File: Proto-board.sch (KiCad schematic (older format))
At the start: 82 parts, among them J1 Conn_01x02, J2 Conn_01x06, J3 Conn_01x05, J4 Conn_01x05, J5 Conn_01x05, J6 Conn_01x05, J7 Conn_01x16, J9 Conn_02x06_Odd_Even, SW1 9001-XX-00, SW10 9001-XX-00, SW11 9001-XX-00, SW12 9001-XX-00, SW13 9001-XX-00, SW14 9001-XX-00, SW15 9001-XX-00, SW16 9001-XX-00, SW17 9001-XX-00, SW18 9001-XX-00, SW19 9001-XX-00, SW2 9001-XX-00, SW20 9001-XX-00, SW3 9001-XX-00, SW4 9001-XX-00, SW5 9001-XX-00, SW6 9001-XX-00, SW7 9001-XX-00, SW8 9001-XX-00, SW9 9001-XX-00, U1 TPL7407LA, U2 MAX17502, U3 XC2C128-VQ100, U4 TPL7407LA, U5 TPL7407LA, U6 MAX15027

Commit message: Final version of protoboard prior to major revision.
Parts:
- added TPA1, TPA2, TPB1, TPB2, TPC1, TPC2, TPD1, TPD2: TEST, Measurement_Points:Measurement_Point_Round-TH_Small, symbol TEST
- C1, C11, C12, C13, C14, C18, C2, C3, C4, C5, C6: footprint Capacitors_SMD:C_1206_HandSoldering -> passives_IKM:1206_PROTO
- J7: footprint Pin_Headers:Pin_Header_Straight_1x16_Pitch2.54mm -> Pin_Headers:Pin_Header_Straight_2x08_Pitch2.00mm_SMD
- L1: footprint Inductors_SMD:L_Coilcraft_XAL5030 -> coilcraft_IKM:LPS6235
- R1, R2, R3, R4: footprint Resistors_SMD:R_1206_HandSoldering -> Resistors_SMD:R_0805
- U2: footprint Housings_DFN_QFN:DFN-10-1EP_3x3mm_Pitch0.5mm -> Housings_DFN_QFN:DFN-10-1EP_2x3mm_Pitch0.5mm
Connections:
- net GNDREF: no longer J3.5 (Pin_5), J4.5 (Pin_5), J5.5 (Pin_5), J6.5 (Pin_5)
- new net GNDS: J3.5 (Pin_5), J4.5 (Pin_5), J5.5 (Pin_5), J6.5 (Pin_5)
- new net TA+: TPA1.1, TPA2.1
- new net TA-: TPB1.1, TPB2.1
- new net TB+: TPC1.1, TPC2.1
- new net TB-: TPD1.1, TPD2.1
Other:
- note added: "Perhaps need to add 100 ohm \nfeedback resistor from 3V3 to FB/VO\n\nMay consider LC filter(s)\n\nLook at INPUT noise from PS"

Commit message: Second version (4x6 card) revC, which was ordered.
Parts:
- removed D11, D12, D13, D14, D15, D16, D17, D18, D19, D20: LED, LEDs:LED_0603_HandSoldering, symbol LED
- removed J1: Conn_01x02, Pin_Headers:Pin_Header_Straight_1x02_Pitch2.54mm, symbol Conn_01x02
- removed J3, J4, J5, J6: Conn_01x05, Pin_Headers:Pin_Header_Straight_1x05_Pitch2.54mm, symbol Conn_01x05
- removed J7: Conn_01x16, Pin_Headers:Pin_Header_Straight_2x08_Pitch2.00mm_SMD, symbol Conn_01x16
- removed J9: Conn_02x06_Odd_Even, Pin_Headers:Pin_Header_Straight_2x06_Pitch2.54mm, symbol Conn_02x06_Odd_Even
- removed RN3: R_Pack08, resistor_array_IKM:SOIC-16, symbol R_Pack08
- added C20, C21, C22: 0.1uF, passives_IKM:1206_PROTO, symbol C
- added C23, C24: CP, Capacitors_SMD:CP_Elec_6.3x4.5, symbol CP
- added J1, J3, J8, J9: Conn_01x08, Connectors_IDC:IDC-Header_2x04_Pitch2.54mm_Straight, symbol Conn_01x08
- added J11, J12, J13, J14, J15, J16, J17, J19: Conn_01x02, Pin_Headers:Pin_Header_Straight_1x02_Pitch2.54mm, symbol Conn_01x02
- added J18: DB37_Female, dsub_IKM:DC37_F_Straddle, symbol DB37_Female
- added J4: Conn_02x20_Odd_Even, Connectors_IDC:IDC-Header_2x20_Pitch2.54mm_Angled, symbol Conn_02x20_Odd_Even
- added J5: Conn_02x08_Odd_Even, Pin_Headers:Pin_Header_Straight_2x08_Pitch2.54mm, symbol Conn_02x08_Odd_Even
- added J6: Conn_02x13_Odd_Even, Pin_Headers:Pin_Header_Straight_2x13_Pitch2.54mm, symbol Conn_02x13_Odd_Even
- added L2, L3: LPS6235-153, coilcraft_IKM:LPS6235, symbol L_Small
- added SW21, SW22, SW23, SW24, SW25, SW26, SW27, SW28, SW29, SW30, SW31, SW32, SW33, SW34, SW35, SW36, SW37, SW38, SW39, SW40: 9001-XX-00, relay_IKM:SIP-4, symbol 9001-XX-00
- added U7, U8, U9: TPL7407LA, Housings_SSOP:TSSOP-16_4.4x5mm_Pitch0.65mm, symbol TPL7407LA
- C19: footprint Capacitors_SMD:CP_Elec_8x5.4 -> Capacitors_SMD:CP_Elec_6.3x4.5
- U2: value MAX17502 -> MAX17502G
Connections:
- net VCCJTAG is gone; now on net 3V3: C14.1, J2.6 (Pin_6), U3.5 (VCCAUX)
- net 3V3: now also C23.1, J4.31 (Pin_31), J4.32 (Pin_32), J6.17 (Pin_17), J6.18 (Pin_18); no longer C10.1, L1.2, U2.5 (FB/VO)
- net CS: now also J5.1 (Pin_1), J5.11 (Pin_11), J5.13 (Pin_13), J5.15 (Pin_15), J5.3 (Pin_3), J5.5 (Pin_5), J5.7 (Pin_7), J5.9 (Pin_9)
- net GND: now also C10.2, C20.2, C21.2, C22.2, C24.2, J6.21 (Pin_21), J6.22 (Pin_22), L3.2, U7.8 (GND), U8.8 (GND), U9.8 (GND); no longer C19.2
- net GNDREF: now also U6.4 (IC), C23.2, J4.11 (Pin_11), J4.12 (Pin_12), J4.21 (Pin_21), J4.22 (Pin_22), J4.3 (Pin_3), J4.33 (Pin_33), J4.34 (Pin_34), J4.4 (Pin_4), J6.19 (Pin_19), J6.20 (Pin_20); no longer C10.2
- net GNDS: now also J18.17
- net LED1.1: now also RN1.8 (R8.1), U3.52 (IO-FB8); no longer RN1.1 (R1.1), U3.39 (IO-FB4)
- net LED1.2: now also RN1.7 (R7.1), U3.53 (IO-FB8); no longer RN1.2 (R2.1), U3.37 (IO-FB4)
- net LED1.3: now also RN1.6 (R6.1), U3.54 (IO-FB6); no longer RN1.3 (R3.1), U3.36 (IO-FB4)
- net LED1.4: now also RN1.5 (R5.1), U3.55 (IO-FB6); no longer RN1.4 (R4.1), U3.35 (IO-FB4)
- net LED2.1: now also RN1.4 (R4.1), U3.56 (IO-FB6); no longer RN1.5 (R5.1), U3.34 (IO-FB4)
- net LED2.2: now also RN1.3 (R3.1), U3.58 (IO-FB6); no longer RN1.6 (R6.1), U3.33 (IO-FB4)
- net LED2.3: now also RN1.2 (R2.1), U3.59 (IO-FB6); no longer RN1.7 (R7.1), U3.32 (IO-FB4)
- net LED2.4: now also RN1.1 (R1.1), U3.60 (IO-FB6); no longer RN1.8 (R8.1), U3.30 (IO-FB4)
- net LED3.1: now also RN2.8 (R8.1), U3.61 (IO-FB6); no longer RN2.1 (R1.1), U3.29 (IO-FB4)
- net LED3.2: now also RN2.7 (R7.1), U3.63 (IO-FB6); no longer RN2.2 (R2.1), U3.28 (IO-FB4(DGE))
- net VCC: now also C10.1, L1.2, U2.5 (FB/VO), C20.1, C21.1, C22.1, J6.23 (Pin_23), J6.24 (Pin_24), SW21.2, SW22.2, SW23.2, SW24.2, SW25.2, SW26.2, SW27.2, SW28.2, SW29.2, SW30.2, SW31.2, SW32.2, SW33.2, SW34.2, SW35.2, SW36.2, SW37.2, SW38.2, SW39.2, SW40.2, U7.9 (COM), U8.9 (COM), U9.9 (COM); no longer C19.1, C7.1, R1.2, U2.2 (VIN)
- net SW34: now reaches U5.10 (OUT7)
- net SW34: now also SW34.3
- net CTRL34: now reaches U5.7 (IN7)
- net CTRL34: now also U3.80 (IO-FB7)
- net vccgood: now reaches U3.46 (IO-FB8)
- net vccgood: now also U2.8 (nRESET)
- net CTRL16: now reaches U3.64 (IO-FB6)
- net CTRL16: now also U1.7 (IN7)
- net CTRL21: now reaches U3.1 (IO-FB3(GOE))
- net CTRL21: now also U8.5 (IN5)
- net CTRL5: now reaches U3.2 (IO-FB3(GOE))
- net CTRL5: now also U8.4 (IN4)
- net CTRL28: now reaches U3.3 (IO-FB1(GOE))
- net CTRL28: now also U8.3 (IN3)
- net CTRL27: now reaches U3.4 (IO-FB1(GOE))
- net CTRL27: now also U8.2 (IN2)
- net CTRL40: now reaches U3.65 (IO-FB5)
- net CTRL40: now also U1.6 (IN6)
- net CTRL15: now reaches U3.66 (IO-FB5)
- net CTRL15: now also U1.5 (IN5)
- net CTRL39: now reaches U3.67 (IO-FB5)
- net CTRL39: now also U1.4 (IN4)
- net CTRL14: now reaches U3.68 (IO-FB5)
- net CTRL14: now also U1.3 (IN3)
- net CTRL13: now reaches U3.70 (IO-FB5)
- net CTRL13: now also U1.2 (IN2)
- net CTRL38: now reaches U3.71 (IO-FB5)
- net CTRL38: now also U1.1 (IN1)
- net CTRL37: now reaches U3.72 (IO-FB5)
- net CTRL37: now also U4.7 (IN7)
- net CTRL36: now reaches U3.73 (IO-FB5)
- net CTRL36: now also U4.6 (IN6)
- net CTRL17: now reaches U3.74 (IO-FB5)
- net CTRL17: now also U4.5 (IN5)
- net CTRL12: now reaches U3.76 (IO-FB5)
- net CTRL12: now also U4.4 (IN4)
- net CTRL35: now reaches U3.77 (IO-FB7)
- net CTRL35: now also U4.3 (IN3)
- net CTRL18: now reaches U3.78 (IO-FB7)
- net CTRL18: now also U4.2 (IN2)
- net CTRL11: now reaches U3.79 (IO-FB7)
- net CTRL11: now also U4.1 (IN1)
- net CTRL19: now reaches U3.81 (IO-FB7)
- net CTRL19: now also U5.6 (IN6)
- net CTRL10: now reaches U3.82 (IO-FB7)
- net CTRL10: now also U5.5 (IN5)
- net CTRL29: now reaches U3.99 (IO-FB3(GSR))
- net CTRL29: now also U8.6 (IN6)
- net at D4.1 (K): now also RN1.12 (R5.2); no longer RN1.13 (R4.2)
- net at D3.1 (K): now also RN1.11 (R6.2); no longer RN1.14 (R3.2)
- net at D2.1 (K): now also RN1.10 (R7.2); no longer RN1.15 (R2.2)
- net at D1.1 (K): now also RN1.9 (R8.2); no longer RN1.16 (R1.2)
- net at D10.1 (K): now also RN2.10 (R7.2); no longer RN2.15 (R2.2)
- net at D9.1 (K): now also RN2.9 (R8.2); no longer RN2.16 (R1.2)
- net at D8.1 (K): now also RN1.16 (R1.2); no longer RN1.9 (R8.2)
- net at D7.1 (K): now also RN1.15 (R2.2); no longer RN1.10 (R7.2)
- net at D6.1 (K): now also RN1.14 (R3.2); no longer RN1.11 (R6.2)
- net at D5.1 (K): now also RN1.13 (R4.2); no longer RN1.12 (R5.2)
- net CTRL1.1 renamed CTRL33
- net CTRL33: now also U5.4 (IN4); no longer U1.7 (IN7)
- net CTRL1.2 renamed CTRL20
- net CTRL20: now also U5.3 (IN3); no longer U1.6 (IN6)
- net CTRL1.3 renamed CTRL9
- net CTRL9: now also U5.2 (IN2); no longer U1.5 (IN5)
- net CTRL1.4 renamed CTRL32
- net CTRL32: now also U5.1 (IN1); no longer U1.4 (IN4)
- net CTRL2.1 renamed CTRL24
- net CTRL24: now also U7.7 (IN7); no longer U1.3 (IN3)
- net CTRL2.2 renamed CTRL8
- net CTRL8: now also U7.6 (IN6); no longer U1.2 (IN2)
- net CTRL2.3 renamed CTRL31
- net CTRL31: now also U7.5 (IN5); no longer U1.1 (IN1)
- net CTRL2.4 renamed CTRL23
- net CTRL23: now also U7.4 (IN4); no longer U4.7 (IN7)
- net CTRL3.1 renamed CTRL7
- net CTRL7: now also U7.3 (IN3); no longer U4.6 (IN6)
- net CTRL3.2 renamed CTRL30
- net CTRL30: now also U7.2 (IN2); no longer U4.5 (IN5)
- net CTRL3.3 renamed CTRL22
- net CTRL22: now also U7.1 (IN1); no longer U4.4 (IN4)
- net CTRL3.4 renamed CTRL6
- net CTRL6: now also U8.7 (IN7); no longer U4.3 (IN3)
- net CTRL4.1 renamed CTRL26
- net CTRL26: now also U8.1 (IN1); no longer U4.2 (IN2)
- net CTRL4.2 renamed CTRL25
- net CTRL25: now also U9.7 (IN7); no longer U4.1 (IN1)
- net CTRL4.3 renamed CTRL4
- net CTRL4: now also U9.6 (IN6); no longer U5.6 (IN6)
- net CTRL4.4 renamed CTRL3
- net CTRL3: now also U9.5 (IN5); no longer U5.5 (IN5)
- net CTRL5.1 renamed CTRL2
- net CTRL2: now also U9.4 (IN4); no longer U5.4 (IN4)
- net CTRL5.2 renamed CTRL1
- net CTRL1: now also U9.3 (IN3); no longer U5.3 (IN3)
- net CTRL5.3 renamed HOLD0
- net HOLD0: now also J6.1 (Pin_1); no longer U5.2 (IN2)
- net CTRL5.4 renamed HOLD1
- net HOLD1: now also J6.3 (Pin_3); no longer U5.1 (IN1)
- net LED3.3: no longer names the net of U3.27 (IO-FB2(GCLK))
- net LED3.3: no longer RN2.3 (R3.1)
- net LED3.4: no longer names the net of U3.24 (IO-FB2(CDR))
- net LED3.4: no longer RN2.4 (R4.1)
- net LED4.1: no longer names the net of U3.23 (IO-FB2(GCLK))
- net LED4.1: no longer RN2.5 (R5.1)
- net LED4.2: no longer names the net of U3.22 (IO-FB2(GCLK))
- net LED4.2: no longer RN2.6 (R6.1)
- net LED4.3 renamed HOLD7
- net HOLD7: now also J6.15 (Pin_15); no longer RN2.7 (R7.1)
- net LED4.4 renamed HOLD6
- net HOLD6: now also J6.13 (Pin_13); no longer RN2.8 (R8.1)
- net LED5.1 renamed HOLD5
- net HOLD5: now also J6.11 (Pin_11)
- net LED5.2 renamed HOLD4
- net HOLD4: now also J6.9 (Pin_9)
- net LED5.3 renamed HOLD3
- net HOLD3: now also J6.7 (Pin_7)
- net LED5.4 renamed HOLD2
- net HOLD2: now also J6.5 (Pin_5)
- net MISO renamed MISO0
- net MISO0: now also J4.7 (Pin_7)
- net MOSI renamed MOSI0
- net MOSI0: now also J4.6 (Pin_6)
- net SCLK renamed SCLK0
- net SCLK0: now also J4.5 (Pin_5)
- net SS1.1 renamed C1ASRC
- net C1ASRC: now also J18.1
- net SS1.2 renamed C1ASNS
- net C1ASNS: now also J18.20
- net SS1.3 renamed A1ASRC
- net A1ASRC: now also J11.1 (Pin_1), J18.2
- net SS1.4 renamed A1ASNS
- net A1ASNS: now also J11.2 (Pin_2), J18.21
- net SS2.1 renamed C2ASRC
- net C2ASRC: now also J18.3
- net SS2.2 renamed C2ASNS
- net C2ASNS: now also J18.22
- net SS2.3 renamed A2ASRC
- net A2ASRC: now also J12.1 (Pin_1), J18.4
- net SS2.4 renamed A2ASNS
- net A2ASNS: now also J12.2 (Pin_2), J18.23
- net SS3.1 renamed C3ASRC
- net C3ASRC: now also J18.5
- net SS3.2 renamed C3ASNS
- net C3ASNS: now also J18.24
- net SS3.3 renamed A3ASRC
- net A3ASRC: now also J13.1 (Pin_1), J18.6
- net SS3.4 renamed A3ASNS
- net A3ASNS: now also J13.2 (Pin_2), J18.25
- net SS4.1 renamed C4ASRC
- net C4ASRC: now also J18.7
- net SS4.2 renamed C4ASNS
- net C4ASNS: now also J18.26
- net SS4.3 renamed A4ASRC
- net A4ASRC: now also J14.1 (Pin_1), J18.8
- net SS4.4 renamed A4ASNS
- net A4ASNS: now also J14.2 (Pin_2), J18.27
- net SS_A renamed CASRC
- net CASRC: now also J1.1 (Pin_1), J1.2 (Pin_2), J8.1 (Pin_1), J8.2 (Pin_2)
- net SS_B renamed CASNS
- net CASNS: now also J1.3 (Pin_3), J1.4 (Pin_4), J8.3 (Pin_3), J8.4 (Pin_4)
- net SS_C renamed AASRC
- net AASRC: now also J1.7 (Pin_7), J1.8 (Pin_8), J8.7 (Pin_7), J8.8 (Pin_8)
- net SS_D renamed AASNS
- net AASNS: now also J1.5 (Pin_5), J1.6 (Pin_6), J8.5 (Pin_5), J8.6 (Pin_6)
- net SW1.1 renamed SW1
- net SW1: now also U9.14 (OUT3); no longer U1.10 (OUT7)
- net SW1.2 renamed SW2
- net SW2: now also U9.13 (OUT4); no longer U1.11 (OUT6)
- net SW1.3 renamed SW15
- net SW15: now also SW15.3; no longer SW3.3
- net SW1.4 renamed SW39
- net SW39: now also SW39.3; no longer SW4.3
- net SW2.1 renamed SW14
- net SW14: now also SW14.3; no longer SW5.3
- net SW2.2 renamed SW13
- net SW13: now also SW13.3; no longer SW6.3
- net SW2.3 renamed SW38
- net SW38: now also SW38.3; no longer SW7.3
- net SW2.4 renamed SW37
- net SW37: now also SW37.3; no longer SW8.3
- net SW3.1 renamed SW36
- net SW36: now also SW36.3; no longer SW9.3
- net SW3.2 renamed SW10
- net SW10: now also U5.12 (OUT5); no longer U4.12 (OUT5)
- net SW3.3 renamed SW11
- net SW11: now also U4.16 (OUT1); no longer U4.13 (OUT4)
- net SW3.4 renamed SW12
- net SW12: now also U4.13 (OUT4); no longer U4.14 (OUT3)
- net SW4.1 renamed SW18
- net SW18: now also SW18.3; no longer SW13.3
- removed net SW4.2: SW14.3, U4.16 (OUT1)
- net SW4.3 renamed SW19
- net SW19: now also SW19.3; no longer SW15.3
- net SW4.4 renamed SW16
- net SW16: now also U1.10 (OUT7); no longer U5.12 (OUT5)
- net SW5.1 renamed SW17
- net SW17: now also U4.12 (OUT5); no longer U5.13 (OUT4)
- net SW5.2 renamed SW20
- net SW20: now also SW20.3; no longer SW18.3
- net SW5.3 renamed SW9
- net SW9: now also SW9.3; no longer SW19.3
- net SW5.4 renamed SW32
- net SW32: now also SW32.3; no longer SW20.3
- net SX_A renamed CBSRC
- net CBSRC: now also J9.1 (Pin_1), J9.2 (Pin_2), SW21.1, SW25.1, SW29.1, SW33.1, SW37.1
- net SX_B renamed CBSNS
- net CBSNS: now also J9.3 (Pin_3), J9.4 (Pin_4), SW22.1, SW26.1, SW30.1, SW34.1, SW38.1
- net SX_C renamed ABSRC
- net ABSRC: now also J9.7 (Pin_7), J9.8 (Pin_8), SW23.1, SW27.1, SW31.1, SW35.1, SW39.1
- net SX_D renamed ABSNS
- net ABSNS: now also J9.5 (Pin_5), J9.6 (Pin_6), SW24.1, SW28.1, SW32.1, SW36.1, SW40.1
- new net 24+: C24.1, C7.1, J6.25 (Pin_25), J6.26 (Pin_26), L2.2, R1.2, U2.2 (VIN)
- new net 24+S: C19.1, J4.35 (Pin_35), J4.36 (Pin_36), J4.37 (Pin_37), L2.1
- new net 24-S: C19.2, J4.38 (Pin_38), J4.39 (Pin_39), J4.40 (Pin_40), L3.1
- new net A1BSNS: J15.2 (Pin_2), J18.29, SW28.4
- new net A1BSRC: J15.1 (Pin_1), J18.10, SW27.4
- new net A2BSNS: J16.2 (Pin_2), J18.31, SW32.4
- new net A2BSRC: J16.1 (Pin_1), J18.12, SW31.4
- new net A3BSNS: J17.2 (Pin_2), J18.33, SW36.4
- new net A3BSRC: J17.1 (Pin_1), J18.14, SW35.4
- new net A4BSNS: J18.35, J19.2 (Pin_2), SW40.4
- new net A4BSRC: J18.16, J19.1 (Pin_1), SW39.4
- new net APDSNS: J18.19, J3.5 (Pin_5), J3.6 (Pin_6), SW24.4
- new net APDSRC: J18.37, J3.7 (Pin_7), J3.8 (Pin_8), SW23.4
- new net C1BSNS: J18.28, SW26.4
- new net C1BSRC: J18.9, SW25.4
- new net C2BSNS: J18.30, SW30.4
- new net C2BSRC: J18.11, SW29.4
- new net C3BSNS: J18.32, SW34.4
- new net C3BSRC: J18.13, SW33.4
- new net C4BSNS: J18.34, SW38.4
- new net C4BSRC: J18.15, SW37.4
- new net CPDSNS: J18.18, J3.3 (Pin_3), J3.4 (Pin_4), SW22.4
- new net CPDSRC: J18.36, J3.1 (Pin_1), J3.2 (Pin_2), SW21.4
- new net CS0: J4.13 (Pin_13), J5.2 (Pin_2)
- new net CS1: J4.14 (Pin_14), J5.4 (Pin_4)
- new net CS2: J4.15 (Pin_15), J5.6 (Pin_6)
- new net CS3: J4.16 (Pin_16), J5.8 (Pin_8)
- new net CS4: J4.17 (Pin_17), J5.10 (Pin_10)
- new net CS5: J4.18 (Pin_18), J5.12 (Pin_12)
- new net CS6: J4.19 (Pin_19), J5.14 (Pin_14)
- new net CS7: J4.20 (Pin_20), J5.16 (Pin_16)
- new net ENABLE0: J6.2 (Pin_2), U3.29 (IO-FB4)
- new net ENABLE1: J6.4 (Pin_4), U3.30 (IO-FB4)
- new net ENABLE2: J6.6 (Pin_6), U3.32 (IO-FB4)
- new net ENABLE3: J6.8 (Pin_8), U3.33 (IO-FB4)
- new net ENABLE4: J6.10 (Pin_10), U3.34 (IO-FB4)
- new net ENABLE5: J6.12 (Pin_12), U3.35 (IO-FB4)
- new net ENABLE6: J6.14 (Pin_14), U3.36 (IO-FB4)
- new net ENABLE7: J6.16 (Pin_16), U3.37 (IO-FB4)
- new net INT0: J4.23 (Pin_23)
- new net INT1: J4.24 (Pin_24)
- new net INT2: J4.25 (Pin_25)
- new net INT3: J4.26 (Pin_26)
- new net INT4: J4.27 (Pin_27)
- new net MISO1: J4.10 (Pin_10)
- new net MOSI1: J4.9 (Pin_9)
- new net RESET: J4.28 (Pin_28)
- new net SCL: J4.2 (Pin_2)
- new net SCLK1: J4.8 (Pin_8)
- new net SDA: J4.1 (Pin_1)
- new net SHTDN: J4.29 (Pin_29)
- new net SHTDN_RDY: J4.30 (Pin_30)
- new net SW21: SW21.3, U8.12 (OUT5)
- new net SW22: SW22.3, U7.16 (OUT1)
- new net SW23: SW23.3, U7.13 (OUT4)
- new net SW24: SW24.3, U7.10 (OUT7)
- new net SW25: SW25.3, U9.10 (OUT7)
- new net SW26: SW26.3, U8.16 (OUT1)
- new net SW27: SW27.3, U8.15 (OUT2)
- new net SW28: SW28.3, U8.14 (OUT3)
- new net SW29: SW29.3, U8.11 (OUT6)
- new net SW3: SW3.3, U9.12 (OUT5)
- new net SW30: SW30.3, U7.15 (OUT2)
- new net SW31: SW31.3, U7.12 (OUT5)
- new net SW33: SW33.3, U5.13 (OUT4)
- new net SW35: SW35.3, U4.14 (OUT3)
- new net SW4: SW4.3, U9.11 (OUT6)
- new net SW40: SW40.3, U1.11 (OUT6)
- new net SW5: SW5.3, U8.13 (OUT4)
- new net SW6: SW6.3, U8.10 (OUT7)
- new net SW7: SW7.3, U7.14 (OUT3)
- new net SW8: SW8.3, U7.11 (OUT6)
- no-connect marks 14 -> 5
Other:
- note added: "Chip Select\n"
- note added: "Extension Interface"
- note added: "Follower circuitry support"
- note added: "Interface Header"
- note added: "SMU A Interface"
- note added: "SMU B Interface"
- note added: "UPDATE SCHEMATIC FROM \nCHANGES ON PROTO-BOARD"
- note removed: "4x DUT Interface"
- note removed: "PMOD SPI\nInterface"
- note removed: "Perhaps need to add 100 ohm \nfeedback resistor from 3V3 to FB/VO\n\nMay consider LC filter(s)\n\nLook at INPUT noise from PS"
- note removed: "Test\nSystem\nInterface"
- moved on the sheet: C1, C10, C11, C12, C13, C14, C15, C16, C17, C18, C19, C2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

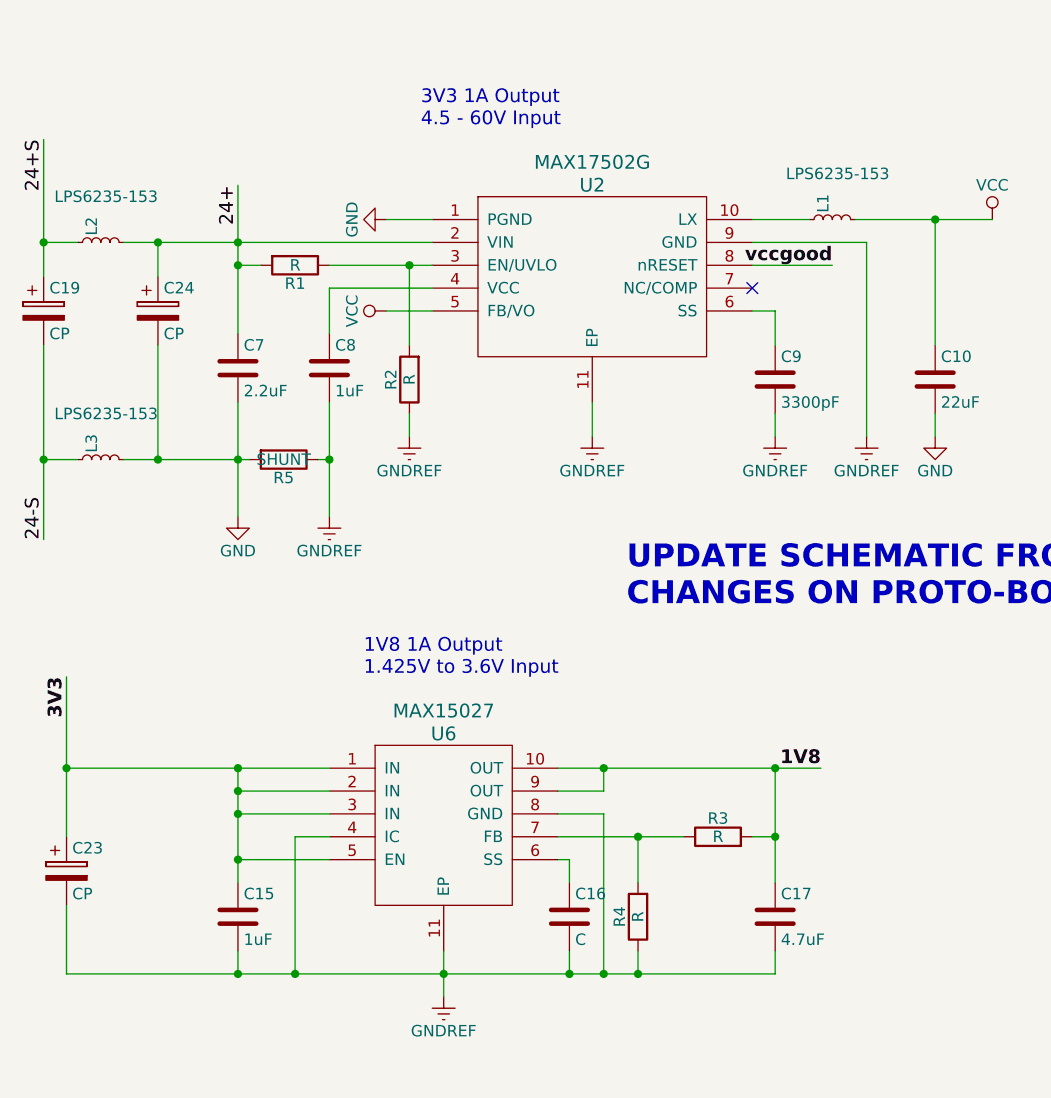
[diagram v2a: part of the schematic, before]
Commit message: First commit to shared repo after board fab and bring-up of 10 boards.
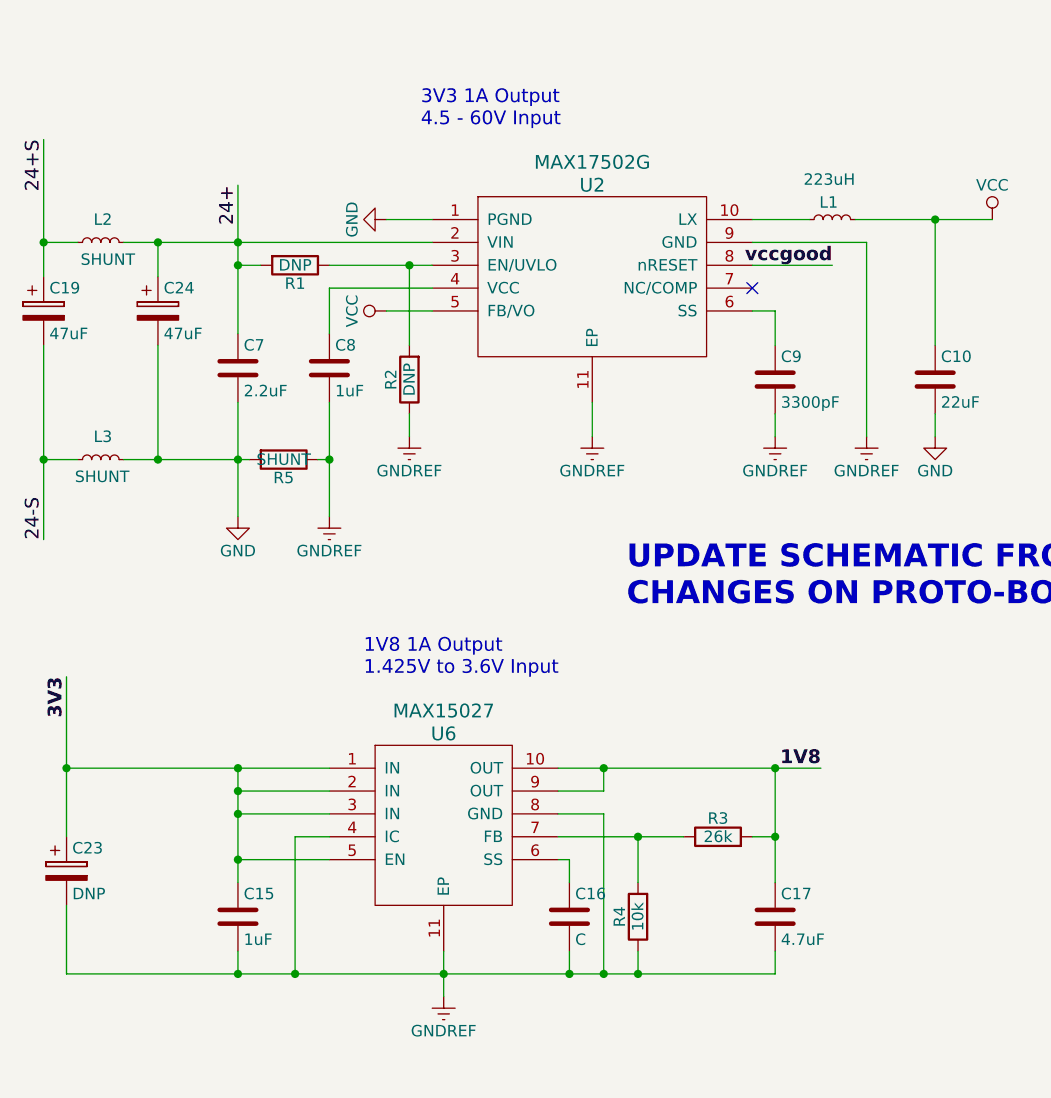
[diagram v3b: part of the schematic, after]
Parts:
- C19, C24: value CP -> 47uF
- C23: value CP -> DNP
- L1: value LPS6235-153 -> 223uH
- L2, L3: value LPS6235-153 -> SHUNT
- R1, R2: value R -> DNP
- R3: value R -> 26k
- R4: value R -> 10k
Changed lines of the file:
@@
 U 1 1 5AD7AE3A
 P 4350 2050
-F 0 "L1" H 4380 2090 50  0000 L CNN
-F 1 "LPS6235-153" V 4550 1800 50  0000 L CNN
+F 0 "L1" V 4425 2025 50  0000 L CNN
+F 1 "223uH" V 4525 1950 50  0000 L CNN
 F 2 "coilcraft_IKM:LPS6235" H 4350 2050 50  0001 C CNN
 F 3 "" H 4350 2050 50  0001 C CNN
@@
 P 2000 2250
 F 0 "R1" V 2080 2250 50  0000 C CNN
-F 1 "R" V 2000 2250 50  0000 C CNN
+F 1 "DNP" V 2000 2250 50  0000 C CNN
 F 2 "Resistors_SMD:R_0805" V 1930 2250 50  0001 C CNN
 F 3 "" H 2000 2250 50  0001 C CNN
@@
 P 2500 2750
 F 0 "R2" V 2580 2750 50  0000 C CNN
-F 1 "R" V 2500 2750 50  0000 C CNN
+F 1 "DNP" V 2500 2750 50  0000 C CNN
 F 2 "Resistors_SMD:R_0805" V 2430 2750 50  0001 C CNN
 F 3 "" H 2500 2750 50  0001 C CNN
@@
 P 3500 5100
 F 0 "R4" V 3580 5100 50  0000 C CNN
-F 1 "R" V 3500 5100 50  0000 C CNN
+F 1 "10k" V 3500 5100 50  0000 C CNN
 F 2 "Resistors_SMD:R_0805" V 3430 5100 50  0001 C CNN
 F 3 "" H 3500 5100 50  0001 C CNN
@@
 P 3850 4750
 F 0 "R3" V 3930 4750 50  0000 C CNN
-F 1 "R" V 3850 4750 50  0000 C CNN
+F 1 "26k" V 3850 4750 50  0000 C CNN
 F 2 "Resistors_SMD:R_0805" V 3780 4750 50  0001 C CNN
 F 3 "" H 3850 4750 50  0001 C CNN
@@
 P 900 2450
 F 0 "C19" H 925 2550 50  0000 L CNN
-F 1 "CP" H 925 2350 50  0000 L CNN
+F 1 "47uF" H 925 2350 50  0000 L CNN
 F 2 "Capacitors_SMD:CP_Elec_6.3x4.5" H 938 2300 50  0001 C CNN
 F 3 "" H 900 2450 50  0001 C CNN
@@
 P 1000 4900
 F 0 "C23" H 1025 5000 50  0000 L CNN
-F 1 "CP" H 1025 4800 50  0000 L CNN
+F 1 "DNP" H 1025 4800 50  0000 L CNN
 F 2 "Capacitors_SMD:CP_Elec_6.3x4.5" H 1038 4750 50  0001 C CNN
 F 3 "" H 1000 4900 50  0001 C CNN
@@
 U 1 1 5B2753B6
 P 1150 2150
-F 0 "L2" H 1180 2190 50  0000 L CNN
-F 1 "LPS6235-153" V 1350 1900 50  0000 L CNN
+F 0 "L2" V 1250 2100 50  0000 L CNN
+F 1 "SHUNT" V 1075 2000 50  0000 L CNN
 F 2 "coilcraft_IKM:LPS6235" H 1150 2150 50  0001 C CNN
 F 3 "" H 1150 2150 50  0001 C CNN
@@
 P 1400 2450
 F 0 "C24" H 1425 2550 50  0000 L CNN
-F 1 "CP" H 1425 2350 50  0000 L CNN
+F 1 "47uF" H 1425 2350 50  0000 L CNN
 F 2 "Capacitors_SMD:CP_Elec_6.3x4.5" H 1438 2300 50  0001 C CNN
 F 3 "" H 1400 2450 50  0001 C CNN
@@
 U 1 1 5B286C0F
 P 1150 3100
-F 0 "L3" H 1180 3140 50  0000 L CNN
-F 1 "LPS6235-153" V 1350 2850 50  0000 L CNN
+F 0 "L3" V 1250 3050 50  0000 L CNN
+F 1 "SHUNT" V 1075 2975 50  0000 L CNN
 F 2 "coilcraft_IKM:LPS6235" H 1150 3100 50  0001 C CNN
 F 3 "" H 1150 3100 50  0001 C CNN
